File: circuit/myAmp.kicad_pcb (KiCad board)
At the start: 2 copper layers, 66 x 72 mm, 49 parts, among them J1 JACK_MONO, J2 HOLE, J3 HOLE, J4 HOLE, J5 HOLE, Q1 J201, Q2 J201, U1 TPA3136D2

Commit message: modular version in beta
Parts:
- added C20: 1nF, myAmp:C_5MM, F.Cu at (92.1, 71.4)
- added C21: 1nF, myAmp:C_5MM, F.Cu at (97.8, 71.8)
- added C22: 100nF, myAmp:C_5MM, F.Cu at (97.2, 36.3)
- added C23: 220μF, myAmp:CPOL_D6.3_P2.5, F.Cu at (142.2, 61.9)
- added C24: 220μF, myAmp:CPOL_D6.3_P2.5, F.Cu at (134.6, 61.9)
- added C25: 330pF, myAmp:C_5MM, F.Cu at (139.4, 97.9)
- added C26: 470pF, myAmp:C_5MM, F.Cu at (139.4, 87.8)
- added C27: 4.7nF, myAmp:C_5MM, F.Cu at (139.4, 78.9)
- added C28: 2.2nF, myAmp:C_5MM, F.Cu at (139.4, 108.1)
- added C29: 100nF, myAmp:C_5MM, F.Cu at (87.6, 59.7)
- added D5: 1N4148, myAmp:DO35, F.Cu at (143.5, 66.3)
- added D6: 1N4148, myAmp:DO35, F.Cu at (133.3, 66.3)
- added J6: HOLE, myAmp:MountingHole, F.Cu at (103.0, 81.0)
- added J7: CONN_01X03, myAmp:SPLITTER, F.Cu at (138.4, 55.5)
- added Q3: BC547, myAmp:TO-92_Inline_Wide, F.Cu at (144.1, 69.5)
- added Q4: BC557, myAmp:TO-92_Inline_Wide, F.Cu at (132.7, 70.1)
- added R11: 1, myAmp:R_10MM, F.Cu at (99.1, 45.8)
- added R12: 1, myAmp:R_10MM, F.Cu at (87.6, 45.8)
- added R15: 4K7, myAmp:R_0805, F.Cu at (146.7, 63.1)
- added R18: 1, myAmp:R_10MM, F.Cu at (105.4, 45.8)
- added R19: 1, myAmp:R_10MM, F.Cu at (95.2, 45.8)
- added R20: 10, myAmp:R_0805, F.Cu at (139.7, 69.5)
- added R21: 10, myAmp:R_0805, F.Cu at (137.2, 69.5)
- added R22: 4K7, myAmp:R_0805, F.Cu at (130.2, 63.1)
- added R23: 100K, myAmp:R_10MM, F.Cu at (142.0, 106.2)
- added R24: 180K, myAmp:R_10MM, F.Cu at (142.0, 93.5)
- added R25: 10K, myAmp:R_10MM, F.Cu at (142.0, 80.8)
- added SW1: OFF ON, myAmp:SW_TINY, F.Cu at (68.6, 115.6)
- added SW2: fender/marshall, myAmp:JUMPER, F.Cu at (121.0, 107.6)
- added U10: PREAMP_CON, myAmp:PREAMP_CON, F.Cu at (104.0, 95.0)
- added U2: TONE_CON, myAmp:TONE_CON, F.Cu at (97.2, 55.5)
- added U3: TL072, myAmp:SOIC-8_3.9x4.9mm_P1.27mm, F.Cu at (87.6, 63.8)
- added U4: TONE_CON, myAmp:TONE_CON, F.Cu at (104.8, 31.8)
- added U5: PREAMP_CON, myAmp:PREAMP_CON, F.Cu at (105.0, 65.7)
- added U6: PREAMP_CON, myAmp:PREAMP_CON, F.Cu at (114.2, 42.0)
- added U7: TLE2426, myAmp:TO-92_Inline_Wide, F.Cu at (83.2, 56.9)
- added U8: TONE_CON, myAmp:TONE_CON, F.Cu at (125.0, 67.1)
- added U9: TONE_CON, myAmp:TONE_CON, F.Cu at (146.7, 80.0)
- C10, C11, C4: footprint myAmp:C_1206 -> myAmp:C_5MM
- C13, C14, C18, C19: value 1uF -> 1μF
- C5, C6: value 47nF -> 100nF; footprint myAmp:C_1206 -> myAmp:C_5MM
- D1, D4: footprint myAmp:LED_D5.0mm -> myAmp:LED_D3.0mm
- J2: value HOLE -> JACK_MONO; footprint myAmp:MountingHole -> myAmp:JACK_CL13106
- L1, L2: footprint myAmp:COILCRAFT_RFS1412 -> myAmp:COILCRAFT_DR0810
- Q1, Q2: value J201 -> MMBFJ201
- R10, R3, R9: footprint myAmp:R_10MM -> myAmp:R_0805
- RV7: value 2K -> 500K; footprint myAmp:RPOT_RKT6V -> myAmp:POT_VULGARIS
- RV8: value 50K -> 250K; footprint myAmp:RPOT_RKT6V -> myAmp:POT_VULGARIS
- moved J2 69.3 mm to (67.3, 65.1), turned to 90 degrees
- moved C5 68.7 mm to (106.0, 36.3), turned to 180 degrees
- moved J5 61.7 mm to (103.0, 115.0)
- moved C10 61.0 mm to (121.0, 114.6)
- moved RV7 58.6 mm to (131.2, 83.3), turned to 270 degrees
- moved RV8 50.8 mm to (131.2, 103.6), turned to 270 degrees
- moved C11 48.1 mm to (121.0, 99.4), turned to 270 degrees
- moved R4 45.6 mm to (121.0, 89.2), turned to 90 degrees
- moved R7 36.9 mm to (108.6, 45.8), turned to 270 degrees
- moved RV1 34.8 mm to (113.4, 70.1), turned to 270 degrees
- moved C6 32.6 mm to (97.2, 59.1), turned to 180 degrees
- moved Q2 31.5 mm to (102.2, 40.8), turned to 0 degrees
- moved D4 29.3 mm to (94.6, 102.9), turned to 90 degrees
- moved D3 28.6 mm to (86.4, 31.9)
- moved J1 28.3 mm to (67.3, 41.4)
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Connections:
- net Net-(D2-Pad2) renamed /guit1
- net PREAMP_OUT renamed Net-(C18-Pad2)
- BT1 pad 1: VDD -> Net-(BT1-Pad1)
- C4 pad 2: /TONE_IN -> Net-(C4-Pad2)
- C6 pad 1: /TONE_OUT -> Net-(C6-Pad1)
- C6 pad 2: Net-(C6-Pad2) -> Net-(C21-Pad1)
- J2 pad 1: Net-(J2-Pad1) -> VGND
- J3 pad 1: Net-(J3-Pad1) -> (no net)
- J4 pad 1: Net-(J4-Pad1) -> (no net)
- J5 pad 1: Net-(J5-Pad1) -> (no net)
- Q1 pad 1: Net-(Q1-Pad1) -> Net-(C22-Pad2)
- Q1 pad 2: /TONE_IN -> Net-(Q1-Pad2)
- Q2 pad 1: Net-(Q2-Pad1) -> Net-(C5-Pad2)
- Q2 pad 2: Net-(C5-Pad2) -> Net-(Q2-Pad2)
- Q2 pad 3: /TONE_OUT -> Net-(Q2-Pad3)
- R4 pad 2: /TONE_IN -> Net-(C4-Pad2)
- R7 pad 1: /TONE_OUT -> Net-(Q2-Pad3)
- RV1 pad 1: Net-(C4-Pad1) -> Net-(C10-Pad1)
- RV1 pad 2: Net-(C6-Pad2) -> Net-(RV1-Pad2)
- RV1 pad 3: Net-(RV1-Pad3) -> Net-(C4-Pad1)
- RV2 pad 1: Net-(C5-Pad1) -> GND
- RV2 pad 3: GND -> Net-(RV2-Pad3)
- RV3 pad 1: Net-(RV1-Pad3) -> Net-(RV3-Pad1)
- RV3 pad 3: Net-(RV3-Pad3) -> Net-(C10-Pad1)
- RV4 pad 1: Net-(RV3-Pad3) -> GND
- RV4 pad 3: GND -> Net-(RV3-Pad1)
- RV5 pad 1: VDD -> VGND
- RV5 pad 2: /TONE_IN -> Net-(C20-Pad2)
- RV5 pad 3: /TONE_IN -> Net-(C20-Pad1)
- RV6 pad 1: VDD -> VGND
- RV6 pad 2: Net-(C5-Pad2) -> Net-(C21-Pad2)
- RV6 pad 3: Net-(C5-Pad2) -> Net-(C21-Pad1)
- RV7 pad 1: Net-(Q1-Pad1) -> Net-(C27-Pad1)
- RV7 pad 2: GND -> Net-(C26-Pad1)
- RV7 pad 3: GND -> Net-(C26-Pad2)
- RV8 pad 1: Net-(Q2-Pad1) -> Net-(C25-Pad2)
- RV8 pad 2: GND -> Net-(R24-Pad2)
- RV8 pad 3: GND -> Net-(C28-Pad1)
- U1 pad 13: Net-(U1-Pad13) -> (no net)
- U1 pad 3: Net-(U1-Pad3) -> (no net)
- U1 pad 4: Net-(U1-Pad4) -> (no net)
- U1 pad 5: Net-(U1-Pad5) -> (no net)
- U1 pad 6: Net-(U1-Pad6) -> (no net)
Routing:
- net VDD: track 177.7 -> 83.3 mm, vias 1 -> 0
- net Net-(C5-Pad2): track 55.9 -> 9.91 mm
- net Net-(C20-Pad1): track 0.00 -> 42.9 mm
- net Net-(C4-Pad1): track 46.1 -> 9.09 mm
- net Net-(R24-Pad2): track 0.00 -> 34.0 mm
- net Net-(C26-Pad2): track 0.00 -> 32.8 mm
- net Net-(C25-Pad1): track 0.00 -> 31.7 mm
- net /TONE_IN: track 29.1 -> 0.00 mm
- net /TONE_OUT: track 26.7 -> 0.00 mm
- net Net-(C10-Pad1): track 36.5 -> 63.0 mm
- net GND: track 28.8 -> 51.0 mm, vias 2 -> 3
- net Net-(C21-Pad1): track 0.00 -> 21.3 mm
- net /guit2: track 0.00 -> 20.4 mm
- net Net-(C26-Pad1): track 0.00 -> 19.3 mm
- net Net-(RV3-Pad1): track 0.00 -> 19.0 mm
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- added copper zone on F.Cu, net GND
- added copper zone on F.Cu, net VDD
- added copper zone on B.Cu, net VGND
- added copper zone on F.Cu, net VGND
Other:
- board size 66 x 72 mm -> 94 x 89 mm
- board text added: "2020 apr 29"
- board text added: "GND"
- board text added: "Mid"
- board text added: "Treb"
- board text added: "VDD"
- board text added: "VGND"
- board text removed: "Middle"
- board text removed: "Treble"
- board text removed: "Volume"

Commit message: sent to fab
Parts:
- moved C26 3.69 mm to (142.2, 90.2)
- moved C25 3.31 mm to (142.2, 99.7)
- moved R25 2.93 mm to (139.1, 80.6)
- moved R23 2.93 mm to (139.1, 106.0)
- moved R24 2.93 mm to (139.1, 93.3)
- moved C27 2.89 mm to (142.2, 78.1)
- moved C28 2.79 mm to (142.2, 108.1)
- moved U10 2.14 mm to (104.8, 97.0)
- moved C5 0.82 mm to (106.7, 36.8)
- moved RV2 0.71 mm to (90.9, 113.2)
- moved C20 0.70 mm to (91.4, 71.1)
- moved U5 0.14 mm to (105.2, 65.6)
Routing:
- net Net-(C22-Pad2): track 18.7 -> 13.2 mm
- net Net-(C26-Pad1): track 19.3 -> 24.7 mm
- net Net-(R24-Pad2): track 34.0 -> 29.6 mm
- net Net-(C28-Pad1): track 9.98 -> 12.9 mm
- net Net-(C25-Pad2): track 11.1 -> 13.1 mm
- net Net-(RV2-Pad3): track 17.8 -> 16.0 mm
- net Net-(C20-Pad1): track 42.9 -> 41.4 mm
- net Net-(C25-Pad1): track 31.7 -> 32.9 mm
- net Net-(C21-Pad1): track 21.3 -> 22.3 mm
- net GND: track 51.0 -> 50.1 mm, vias 3 -> 2
- net VDD: track 83.3 -> 84.2 mm
- net Net-(C26-Pad2): track 32.8 -> 33.6 mm
- net Net-(C5-Pad1): track 7.39 -> 6.63 mm
- net Net-(C4-Pad2): track 17.4 -> 18.2 mm
- net Net-(C20-Pad2): track 15.3 -> 14.6 mm
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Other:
- outline, holes or cut-outs redrawn
- board text added: "2020 may 3"
- board text added: "Vol"
- board text removed: "2020 apr 29"

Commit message: this one was actually sent
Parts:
- added REF**: PIN_1x4, myAmp:PIN_1x4, F.Cu at (120.9, 55.1)
- added REF**: SOIC-8_3.9x4.9mm_P1.27mm, myAmp:SOIC-8_tiny, F.Cu at (117.1, 55.1)
- added REF**: PIN_1x4, myAmp:PIN_1x4, F.Cu at (113.3, 55.1)
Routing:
- net (no net): track 0.00 -> 16.1 mm
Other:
- outline, holes or cut-outs redrawn
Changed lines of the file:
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@@
   (general
     (thickness 1.6)
-    (drawings 114)
-    (tracks 340)
+    (drawings 122)
+    (tracks 356)
     (zones 0)
-    (modules 87)
+    (modules 90)
     (nets 53)
   )
@@
     (add_net VGND)
   )
+  (module myAmp:PIN_1x4 (layer F.Cu)
+    (at 120.89 55.08)
+    (fp_text reference REF** (at -3.81 -3.81 180) (layer Dwgs.User) hide
+      (effects (font (size 0.5 0.5) (thickness 0.1)))
+    )
+    (fp_text value PIN_1x4 (at -3.81 3.81 180) (layer Dwgs.User) hide
+      (effects (font (size 0.5 0.5) (thickness 0.1)))
+    )
+    (pad 1 thru_hole circle (at 0 -3.81) (size 1.1 1.1) (drill 0.8) (layers *.Cu *.Mask))
+    (pad 2 thru_hole circle (at 0 -1.27) (size 1.1 1.1) (drill 0.8) (layers *.Cu *.Mask))
+    (pad 3 thru_hole circle (at 0 1.27) (size 1.1 1.1) (drill 0.8) (layers *.Cu *.Mask))
+    (pad 4 thru_hole circle (at 0 3.81) (size 1.1 1.1) (drill 0.8) (layers *.Cu *.Mask))
+  )
+  (module myAmp:SOIC-8_tiny (layer F.Cu)
+    (at 117.08 55.08)
+    (descr "SOIC, 8 Pin (JEDEC MS-012AA, https://www.analog.com/media/en/package-pcb-resources/package/pkg_pdf/soic_narrow-r/r_8.pdf), generated with kicad-footprint-generator ipc_gullwing_generator.py")
+    (tags "SOIC SO")
+    (attr smd)
+    (fp_text reference REF** (at 0 0 180) (layer F.SilkS) hide
+      (effects (font (size 0.75 0.75) (thickness 0.15)))
+    )
+    (fp_text value SOIC-8_3.9x4.9mm_P1.27mm (at 0 0.635) (layer F.Fab)
+      (effects (font (size 0.03 0.03) (thickness 0.0075)))
+    )
+    (fp_line (start 2.032 2.54) (end -2.032 2.54) (layer F.SilkS) (width 0.15))
+    (fp_line (start -2.032 -2.667) (end 2.032 -2.667) (layer F.SilkS) (width 0.15))
+    (fp_line (start -2.032 -2.413) (end -2.032 -2.667) (layer F.SilkS) (width 0.15))
+    (fp_line (start -2.54 -2.413) (end -2.032 -2.413) (layer F.SilkS) (width 0.15))
+    (fp_text user %R (at 0 0) (layer F.Fab)
+      (effects (font (size 0.03 0.03) (thickness 0.0075)))
+    )
+    (fp_circle (center -1.143 -1.905) (end -0.889 -1.651) (layer F.SilkS) (width 0.15))
+    (fp_line (start -2.032 -1.143) (end -2.032 -1.397) (layer F.SilkS) (width 0.15))
+    (fp_line (start 2.032 -2.413) (end 2.032 -2.667) (layer F.SilkS) (width 0.15))
+    (fp_line (start 2.032 -1.397) (end 2.032 -1.143) (layer F.SilkS) (width 0.15))
+    (fp_line (start 2.032 -0.127) (end 2.032 0.127) (layer F.SilkS) (width 0.15))
+    (fp_line (start 2.032 1.143) (end 2.032 1.397) (layer F.SilkS) (width 0.15))
+    (fp_line (start -2.032 2.54) (end -2.032 2.413) (layer F.SilkS) (width 0.15))
+    (fp_line (start 2.032 2.413) (end 2.032 2.54) (layer F.SilkS) (width 0.15))
+    (fp_line (start -2.032 1.397) (end -2.032 1.143) (layer F.SilkS) (width 0.15))
+    (fp_line (start -2.032 0.127) (end -2.032 -0.127) (layer F.SilkS) (width 0.15))
+    (pad 8 smd roundrect (at 2.5 -1.905) (size 1.2 0.6) (layers F.Cu F.Paste F.Mask) (roundrect_rratio 0.25))
+    (pad 7 smd roundrect (at 2.5 -0.635) (size 1.2 0.6) (layers F.Cu F.Paste F.Mask) (roundrect_rratio 0.25))
+    (pad 6 smd roundrect (at 2.5 0.635) (size 1.2 0.6) (layers F.Cu F.Paste F.Mask) (roundrect_rratio 0.25))
+    (pad 5 smd roundrect (at 2.5 1.905) (size 1.2 0.6) (layers F.Cu F.Paste F.Mask) (roundrect_rratio 0.25))
+    (pad 4 smd roundrect (at -2.5 1.905) (size 1.2 0.6) (layers F.Cu F.Paste F.Mask) (roundrect_rratio 0.25))
+    (pad 3 smd roundrect (at -2.5 0.635) (size 1.2 0.6) (layers F.Cu F.Paste F.Mask) (roundrect_rratio 0.25))
+    (pad 2 smd roundrect (at -2.5 -0.635) (size 1.2 0.6) (layers F.Cu F.Paste F.Mask) (roundrect_rratio 0.25))
+    (pad 1 smd roundrect (at -2.5 -1.905) (size 1.2 0.6) (layers F.Cu F.Paste F.Mask) (roundrect_rratio 0.25))
+    (model ${KISYS3DMOD}/Package_SO.3dshapes/SOIC-8_3.9x4.9mm_P1.27mm.wrl
+      (at (xyz 0 0 0))
+      (scale (xyz 1 1 1))
+      (rotate (xyz 0 0 0))
+    )
+  )
+  (module myAmp:PIN_1x4 (layer F.Cu)
+    (at 113.27 55.08)
+    (fp_text reference REF** (at 3.81 -3.81 180) (layer Dwgs.User) hide
+      (effects (font (size 0.5 0.5) (thickness 0.1)))
+    )
+    (fp_text value PIN_1x4 (at 3.81 3.81 180) (layer Dwgs.User) hide
+      (effects (font (size 0.5 0.5) (thickness 0.1)))
+    )
+    (pad 1 thru_hole circle (at 0 -3.81) (size 1.1 1.1) (drill 0.8) (layers *.Cu *.Mask))
+    (pad 2 thru_hole circle (at 0 -1.27) (size 1.1 1.1) (drill 0.8) (layers *.Cu *.Mask))
+    (pad 3 thru_hole circle (at 0 1.27) (size 1.1 1.1) (drill 0.8) (layers *.Cu *.Mask))
+    (pad 4 thru_hole circle (at 0 3.81) (size 1.1 1.1) (drill 0.8) (layers *.Cu *.Mask))
+  )
   (module myAmp:HTSSOP-28_4.4x9.7mm_Pitch0.65mm_ThermalPad (layer F.Cu)
     (at 84.665 95.24375 180)
@@
     )
   )
+  (gr_line (start 111 51.5) (end 112 51.5) (layer Edge.Cuts) (width 0.05))
+  (gr_line (start 112 51.5) (end 112 50) (layer Edge.Cuts) (width 0.05))
+  (gr_line (start 120.5 60) (end 120.5 61) (layer Edge.Cuts) (width 0.05))
+  (gr_line (start 126 61) (end 122 61) (layer Edge.Cuts) (width 0.05))
+  (gr_line (start 112 60) (end 112 53) (layer Edge.Cuts) (width 0.05))
+  (gr_line (start 120.5 60) (end 112 60) (layer Edge.Cuts) (width 0.05))
+  (gr_line (start 122 50) (end 122 61) (layer Edge.Cuts) (width 0.05))
+  (gr_line (start 112 50) (end 122 50) (layer Edge.Cuts) (width 0.05))
   (gr_text Bass (at 135.128 78.232 90) (layer F.SilkS)
     (effects (font (size 1.5 1.5) (thickness 0.3)))
@@
   (gr_line (start 62.5 76) (end 62.5 77) (layer Edge.Cuts) (width 0.05))
   (gr_line (start 101.5 76) (end 101.5 77) (layer Edge.Cuts) (width 0.05))
-  (gr_line (start 103 53) (end 111 53) (layer Edge.Cuts) (width 0.05))
+  (gr_line (start 103 53) (end 112 53) (layer Edge.Cuts) (width 0.05))
   (gr_line (start 101.5 53) (end 101.5 54) (layer Edge.Cuts) (width 0.05))
   (gr_line (start 55 53) (end 55 54) (layer Edge.Cuts) (width 0.05))
@@
   (gr_line (start 103 69.85) (end 103 77) (layer Edge.Cuts) (width 0.05))
   (gr_line (start 106.9975 69.85) (end 102.9975 69.85) (layer Edge.Cuts) (width 0.05))
-  (gr_line (start 110 61) (end 126 61) (layer Edge.Cuts) (width 0.05))
+  (gr_line (start 110 61) (end 120.5 61) (layer Edge.Cuts) (width 0.05))
   (gr_line (start 111 30) (end 55 30) (layer Edge.Cuts) (width 0.05))
   (gr_line (start 111 36.5) (end 111 30) (layer Edge.Cuts) (width 0.05))
@@
   (gr_line (start 116 46.228) (end 116 36.5) (layer Edge.Cuts) (width 0.05))
   (gr_line (start 111 46.228) (end 116 46.228) (layer Edge.Cuts) (width 0.05))
-  (gr_line (start 111 53) (end 111 46.228) (layer Edge.Cuts) (width 0.05))
+  (gr_line (start 111 51.5) (end 111 46.228) (layer Edge.Cuts) (width 0.05))
   (gr_line (start 56.5 53) (end 101.5 53) (layer Edge.Cuts) (width 0.05))
   (gr_line (start 55 30) (end 55 53) (layer Edge.Cuts) (width 0.05))
@@
   )
   (gr_line (start 55 115) (end 55 81) (layer Edge.Cuts) (width 0.05))
+  (segment (start 114.58 52.58) (end 113.27 51.27) (width 0.508) (layer F.Cu) (net 0))
+  (segment (start 114.58 53.175) (end 114.58 52.58) (width 0.508) (layer F.Cu) (net 0))
+  (segment (start 113.905 54.445) (end 113.27 53.81) (width 0.508) (layer F.Cu) (net 0))
+  (segment (start 114.58 54.445) (end 113.905 54.445) (width 0.508) (layer F.Cu) (net 0))
+  (segment (start 113.905 55.715) (end 113.27 56.35) (width 0.508) (layer F.Cu) (net 0))
+  (segment (start 114.58 55.715) (end 113.905 55.715) (width 0.508) (layer F.Cu) (net 0))
+  (segment (start 114.58 57.58) (end 113.27 58.89) (width 0.508) (layer F.Cu) (net 0))
+  (segment (start 114.58 56.985) (end 114.58 57.58) (width 0.508) (layer F.Cu) (net 0))
+  (segment (start 119.58 57.58) (end 120.89 58.89) (width 0.508) (layer F.Cu) (net 0))
+  (segment (start 119.58 56.985) (end 119.58 57.58) (width 0.508) (layer F.Cu) (net 0))
+  (segment (start 120.255 55.715) (end 120.89 56.35) (width 0.508) (layer F.Cu) (net 0))
+  (segment (start 119.58 55.715) (end 120.255 55.715) (width 0.508) (layer F.Cu) (net 0))
+  (segment (start 120.255 54.445) (end 120.89 53.81) (width 0.508) (layer F.Cu) (net 0))
+  (segment (start 119.58 54.445) (end 120.255 54.445) (width 0.508) (layer F.Cu) (net 0))
+  (segment (start 119.58 52.58) (end 120.89 51.27) (width 0.508) (layer F.Cu) (net 0))
+  (segment (start 119.58 53.175) (end 119.58 52.58) (width 0.508) (layer F.Cu) (net 0))
   (segment (start 83.7525 93.61875) (end 84.24 93.13125) (width 0.4064) (layer F.Cu) (net 1))
   (segment (start 83.7525 96.86875) (end 84.24 97.35625) (width 0.3556) (layer F.Cu) (net 1))

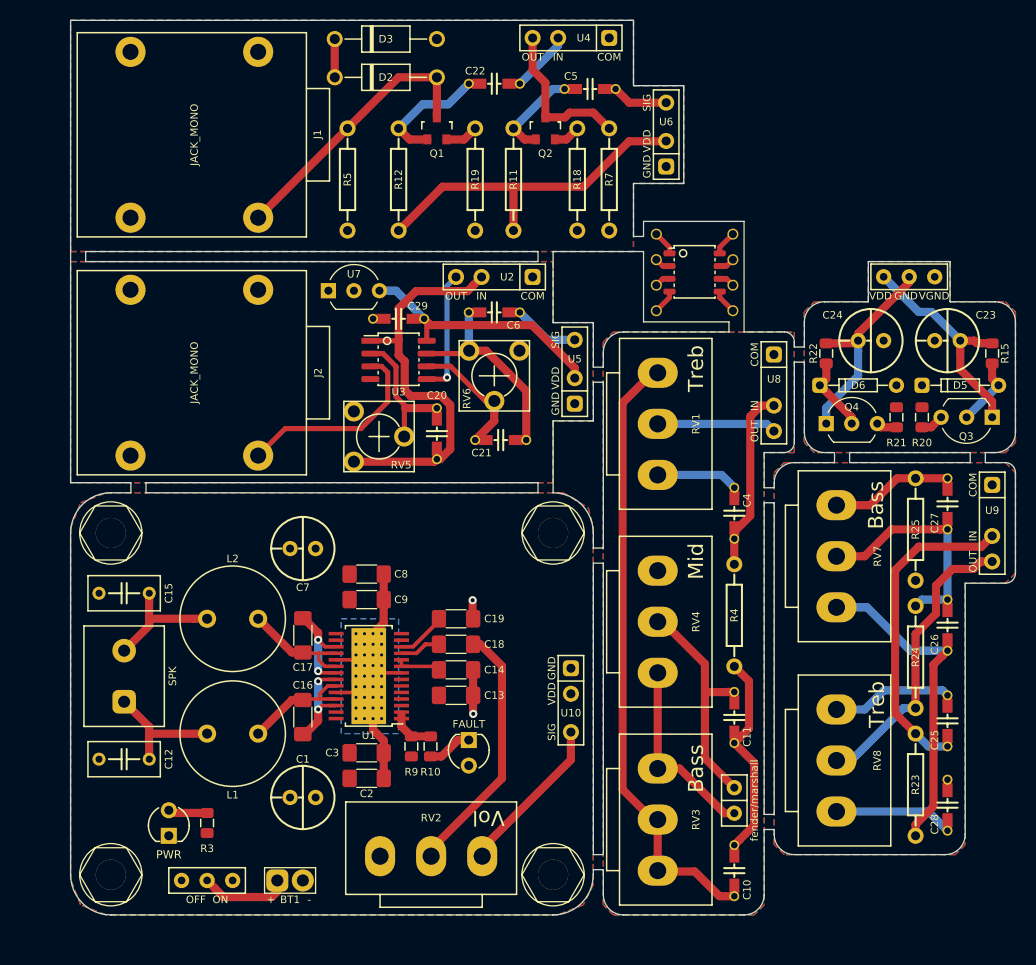
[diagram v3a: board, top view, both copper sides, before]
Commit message: made FV-1 prototype; converted kicad 5 files to kicad 6
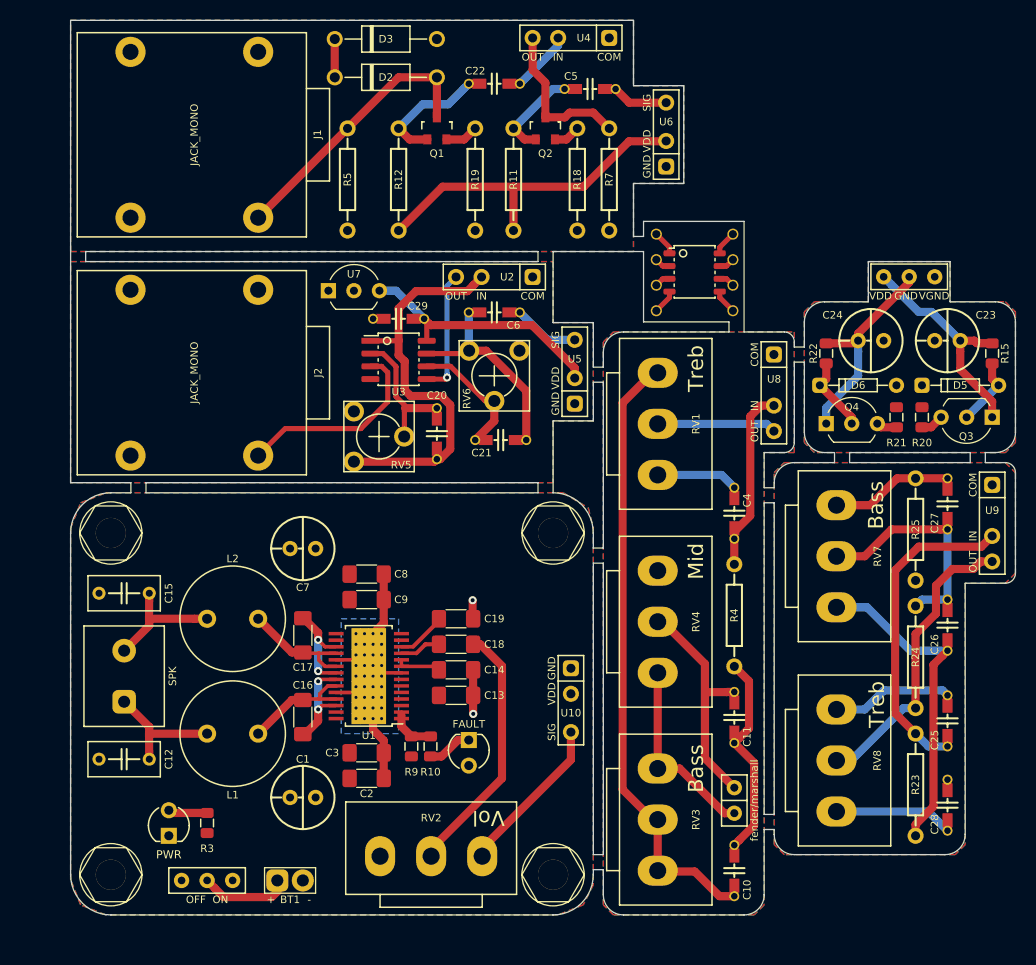
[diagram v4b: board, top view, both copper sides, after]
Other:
- net class Default removed
